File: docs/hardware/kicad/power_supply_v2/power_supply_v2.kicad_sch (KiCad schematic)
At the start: 99 parts, among them J1 Barrel_Jack, J2 LOAD 3V3, J3 LOAD 5V, J4 LOAD Vvar, Q1 MMBT3904LT1G, Q2 AO3401A, SW2 Rotary_Encoder_3_Pin, U1 TPS54302, U14 SHT31-DIS, U15 SHT31-DIS, U2 MCP1700T-3302E/TT, U3 MCP1700T-3302E/TT, U4 TPS54302, U5 MCP1700T-5002E/TT, U6 TPS54302, U7 TPS54302, U8 TPS22917DBV, U9 TPS22917DBV

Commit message: updated schematic for LC filters and added voltage injection to other bucks
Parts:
- removed C11, C18, C9: 1μF, symbol Library:C_Small
- removed D2: B340A-13-F, digikey-footprints:DO-214AC, symbol Library:B340A-13-F
- removed U3: MCP1700T-3302E/TT, digikey-footprints:SOT-23-3, symbol Library:MCP1700T-3302E_TT
- added C10, C19, C32, C33: 10μF, symbol Library:C_Small
- added L2, L4, L7: 1μH, symbol Library:L_Iron
- added R4: 62kR, symbol Library:R_Small_US
- added R9: 82kR, symbol Library:R_Small_US
- R3: value 19kR2 -> 22kR1
- R8: renamed from R7; value 12kR1 -> 13kR3
- renumbered C12 to C11, C13 to C12, C14 to C13, C15 to C14, C16 to C15, C17 to C16, C19 to C17, C20 to C18, C21 to C20, C22 to C21, C23 to C22, C24 to C23, C25 to C24, C26 to C25, C27 to C26, C28 to C27, C29 to C28, C30 to C29, C31 to C30, C32 to C31, C33 to C34, C34 to C35, C35 to C36, C36 to C37, C37 to C38, C38 to C39, C39 to C40, C40 to C41, C41 to C42, C10 to C9, L2 to L3, L3 to L5, L4 to L6, R8 to R10, R9 to R11, R10 to R12, R11 to R13, R12 to R14, R13 to R15, R14 to R16, R15 to R17, R16 to R18, R17 to R19, R18 to R20, R19 to R21, R20 to R22, R21 to R23, R22 to R24, R23 to R25, R24 to R26, R25 to R27, R4 to R5, R5 to R6, R6 to R7
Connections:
- net +3V3B: now also C10.1, L2.2
- net +3V7: now also L2.1
- net +5V5: now also L4.1
- net +5VA: now also C18.1, U5.2 (OUT)
- net +5VB: now also C19.1, L4.2; no longer C18.1, U5.2 (OUT)
- net +V_{VAR}: now also L7.1; no longer Q2.2 (S), R25.2
- net BUCK_12V_EN: now also R11.1; no longer R11.2
- net GNDREF: now also C10.2, C19.2, C32.2, C33.2
- net Microcontroller/BUCK_VVAR_EN_PC5: now also R15.1; no longer R15.2
- net at C7.2, R2.2, R3.1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: now also R4.1
- net at C16.2, R7.2, R8.1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: now also R9.1
- net at U7.5 (EN): now also R15.2; no longer R15.1
- net at U6.5 (EN): now also R11.2; no longer R11.1
- new net: C32.1, C33.1, L7.2, Q2.2 (S), R25.2
- new net DAC_3V7_PA6: R4.2
- new net DAC_5V5_PA5: R9.2
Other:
- sheet Microcontroller ports: added DAC_3V7_PA6, DAC_5V5_PA5; removed none
- note added: "TODO: rework power rails to rely on filtering via inductor and capacitor"
- note removed: "V_{f(MAX)}=0V5"
- moved on the sheet: C17, C18, C8, C9, DS3, DS4, R10, R14, R18, R5, U14, U15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

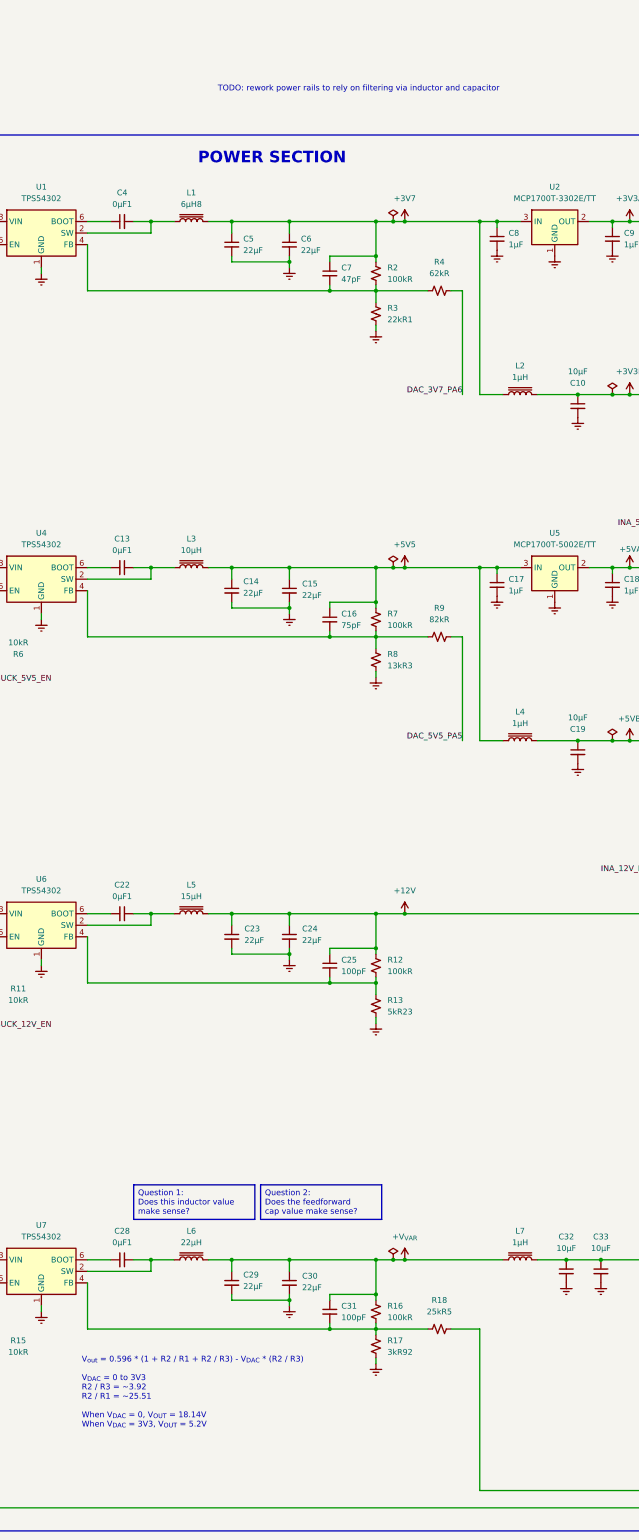
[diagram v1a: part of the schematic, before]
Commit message: rework buck resistor divider values + add fb injection to 3V3 and 5V rail bucks
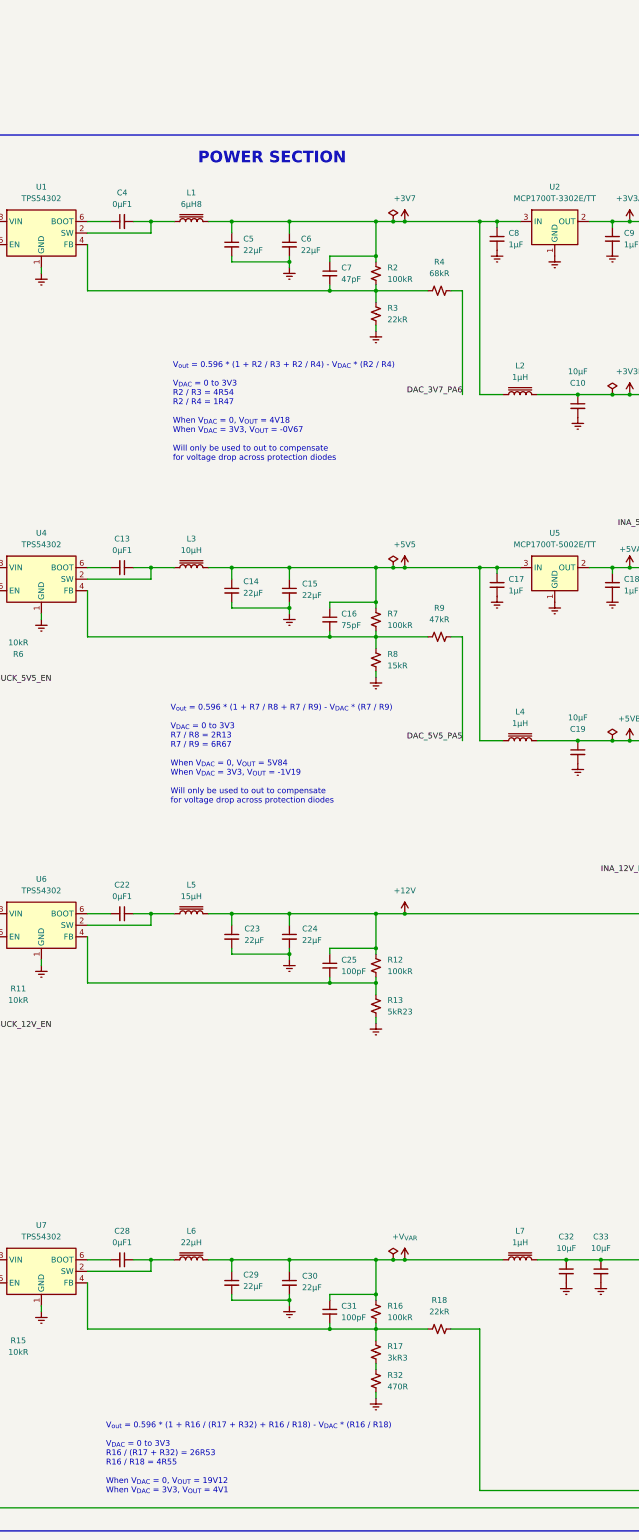
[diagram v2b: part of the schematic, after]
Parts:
- added R32: 470R, symbol Library:R_Small_US
- R17: value 3kR92 -> 3kR3
- R18: value 25kR5 -> 22kR
- R3: value 22kR1 -> 22kR
- R4: value 62kR -> 68kR
- R8: value 13kR3 -> 15kR
- R9: value 82kR -> 47kR
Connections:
- net GNDREF: now also R32.2; no longer R17.2
- new net: R17.2, R32.1
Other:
- note added: "V_{out} = 0.596 * (1 + R16 / (R17 + R32) + R16 / R18) - V_{DAC} * (R16 / R18) V_{DAC} = 0 to 3V3 R16 / (R17 + R32) = 26R53 R16 / R18 = 4R55 When V_{DAC} = 0, V_{OUT} = 19V12 When V_{DAC} = 3V3, V_{OUT} = 4V1"
- note added: "V_{out} = 0.596 * (1 + R2 / R3 + R2 / R4) - V_{DAC} * (R2 / R4) V_{DAC} = 0 to 3V3 R2 / R3 = 4R54 R2 / R4 = 1R47 When V_{DAC} = 0, V_{OUT} = 4V18 When V_{DAC} = 3V3, V_{OUT} = -0V67 Will only be used to out to compensate for voltage drop across protection diodes"
- note added: "V_{out} = 0.596 * (1 + R7 / R8 + R7 / R9) - V_{DAC} * (R7 / R9) V_{DAC} = 0 to 3V3 R7 / R8 = 2R13 R7 / R9 = 6R67 When V_{DAC} = 0, V_{OUT} = 5V84 When V_{DAC} = 3V3, V_{OUT} = -1V19 Will only be used to out to compensate for voltage drop across protection diodes"
- note removed: "TODO: rework power rails to rely on filtering via inductor and capacitor"
- note removed: "V_{out} = 0.596 * (1 + R2 / R1 + R2 / R3) - V_{DAC} * (R2 / R3) V_{DAC} = 0 to 3V3 R2 / R3 = ~3.92 R2 / R1 = ~25.51 When V_{DAC} = 0, V_{OUT} = 18.14V When V_{DAC} = 3V3, V_{OUT} = 5.2V"
- moved on the sheet: R17
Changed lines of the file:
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@@
 	(title_block
 		(title "Digital Variable DC Bench Power Supply")
-		(date "2026-04-27")
-		(rev "1")
+		(date "2026-04-30")
+		(rev "A2")
 	)
 	(rectangle
@@
 		)
 	)
-	(text "V_{out} = 0.596 * (1 + R2 / R1 + R2 / R3) - V_{DAC} * (R2 / R3)\n\nV_{DAC} = 0 to 3V3\nR2 / R3 = ~3.92\nR2 / R1 = ~25.51\n\nWhen V_{DAC} = 0, V_{OUT} = 18.14V\nWhen V_{DAC} = 3V3, V_{OUT} = 5.2V"
+	(text "V_{out} = 0.596 * (1 + R16 / (R17 + R32) + R16 / R18) - V_{DAC} * (R16 / R18)\n\nV_{DAC} = 0 to 3V3\nR16 / (R17 + R32) = 26R53\nR16 / R18 = 4R55\n\nWhen V_{DAC} = 0, V_{OUT} = 19V12\nWhen V_{DAC} = 3V3, V_{OUT} = 4V1"
 		(exclude_from_sim no)
-		(at 124.46 346.71 0)
+		(at 129.794 361.188 0)
 		(effects
 			(font
@@
 		)
 	)
-	(text "TODO: rework power rails to rely on filtering via inductor and capacitor"
-		(exclude_from_sim no)
-		(at 185.42 59.69 0)
-		(effects
-			(font
-				(size 1.27 1.27)
-			)
-		)
-	)
 	(text "V_{f(MAX)}=0V7"
 		(exclude_from_sim no)
@@
 		)
 	)
+	(text "V_{out} = 0.596 * (1 + R2 / R3 + R2 / R4) - V_{DAC} * (R2 / R4)\n\nV_{DAC} = 0 to 3V3\nR2 / R3 = 4R54\nR2 / R4 = 1R47\n\nWhen V_{DAC} = 0, V_{OUT} = 4V18\nWhen V_{DAC} = 3V3, V_{OUT} = -0V67\n\nWill only be used to out to compensate\nfor voltage drop across protection diodes"
+		(exclude_from_sim no)
+		(at 144.526 130.81 0)
+		(effects
+			(font
+				(size 1.27 1.27)
+			)
+			(justify left)
+		)
+	)
 	(text "USER\nINTERFACES"
 		(exclude_from_sim no)
@@
 		)
 	)
+	(text "V_{out} = 0.596 * (1 + R7 / R8 + R7 / R9) - V_{DAC} * (R7 / R9)\n\nV_{DAC} = 0 to 3V3\nR7 / R8 = 2R13\nR7 / R9 = 6R67\n\nWhen V_{DAC} = 0, V_{OUT} = 5V84\nWhen V_{DAC} = 3V3, V_{OUT} = -1V19\n\nWill only be used to out to compensate\nfor voltage drop across protection diodes"
+		(exclude_from_sim no)
+		(at 144.018 206.248 0)
+		(effects
+			(font
+				(size 1.27 1.27)
+			)
+			(justify left)
+		)
+	)
 	(text "No pull-up resistors included for I2C\nbecause the OLED and SHT31s are modules\nwith built-in resistors. May need to\nalter modules or remove the resistors."
 		(exclude_from_sim no)
@@
 		)
 	)
-	(text_box "Question 2:\nDoes the feedforward cap value make sense?"
-		(exclude_from_sim no)
-		(at 163.83 300.99 0)
-		(size 26.67 7.62)
-		(margins 0.9525 0.9525 0.9525 0.9525)
-		(stroke
-			(width 0)
-			(type solid)
-		)
-		(fill
-			(type none)
-		)
-		(effects
-			(font
-				(size 1.27 1.27)
-			)
-			(justify left top)
-		)
-	)
-	(text_box "Question 1:\nDoes this inductor value make sense?"
-		(exclude_from_sim no)
-		(at 135.89 300.99 0)
-		(size 26.67 7.62)
-		(margins 0.9525 0.9525 0.9525 0.9525)
-		(stroke
-			(width 0)
-			(type solid)
-		)
-		(fill
-			(type none)
-		)
-		(effects
-			(font
-				(size 1.27 1.27)
-			)
-			(justify left top)
-		)
-	)
 	(junction
 		(at 539.75 24.13)
@@
 	(wire
 		(pts
+			(xy 189.23 340.36) (xy 189.23 341.63)
+		)
+		(stroke
+			(width 0)
+			(type default)
+		)
+	)
+	(wire
+		(pts
 			(xy 408.94 48.26) (xy 414.02 48.26)
 		)
@@
 	(wire
 		(pts
-			(xy 189.23 332.74) (xy 189.23 334.01)
+			(xy 189.23 332.74) (xy 189.23 335.28)
 		)
 		(stroke
@@
 	(wire
 		(pts
-			(xy 189.23 339.09) (xy 189.23 340.36)
-		)
-		(stroke
-			(width 0)
-			(type default)
-		)
-	)
-	(wire
-		(pts
 			(xy 260.35 165.1) (xy 261.62 165.1)
 		)
@@
 	(wire
 		(pts
+			(xy 189.23 346.71) (xy 189.23 347.98)
+		)
+		(stroke
+			(width 0)
+			(type default)
+		)
+	)
+	(wire
+		(pts
 			(xy 193.04 165.1) (xy 195.58 165.1)
 		)
@@
 	)
 	(symbol
+		(lib_id "Library:R_Small_US")
+		(at 189.23 344.17 0)
+		(unit 1)
+		(exclude_from_sim no)
+		(in_bom yes)
+		(on_board yes)
+		(dnp no)
+		(fields_autoplaced yes)
+		(property "Reference" "R32"
+			(at 191.77 342.8999 0)
+			(effects
+				(font
+					(size 1.27 1.27)
+				)
+				(justify left)
+			)
+		)
+		(property "Value" "470R"
+			(at 191.77 345.4399 0)
+			(effects
+				(font
+					(size 1.27 1.27)
+				)
+				(justify left)
+			)
+		)
+		(property "Footprint" ""
+			(at 189.23 344.17 0)
+			(effects
+				(font
+					(size 1.27 1.27)
+				)
+				(hide yes)
+			)
+		)
+		(property "Datasheet" "~"
+			(at 189.23 344.17 0)
+			(effects
+				(font
+					(size 1.27 1.27)
+				)
+				(hide yes)
+			)
+		)
+		(property "Description" "Resistor, small US symbol"
+			(at 189.23 344.17 0)
+			(effects
+				(font
+					(size 1.27 1.27)
+				)
+				(hide yes)
+			)
+		)
+		(pin "1"
+		)
+		(pin "2"
+		)
+		(instances
+			(project "power_supply_v2"
+				(path "/cac0009d-9d0b-438f-a386-67368a9db47f"
+					(reference "R32")
+					(unit 1)
+				)
+			)
+		)
+	)
+	(symbol
 		(lib_id "power:PWR_FLAG")
 		(at 40.64 43.18 0)
@@
 			)
 		)
-		(property "Value" "22kR1"
+		(property "Value" "22kR"
 			(at 191.77 110.4899 0)
 			(effects
@@
 	(symbol
 		(lib_id "power:GNDREF")
-		(at 189.23 340.36 0)
+		(at 189.23 347.98 0)
 		(unit 1)
 		(exclude_from_sim no)
@@
 		(fields_autoplaced yes)
 		(property "Reference" "#PWR011"
-			(at 189.23 346.71 0)
+			(at 189.23 354.33 0)
 			(effects
 				(font
@@
 		)
 		(property "Value" "GNDREF"
-			(at 189.23 345.44 0)
+			(at 189.23 353.06 0)
 			(effects
 				(font
@@
 		)
 		(property "Footprint" ""
-			(at 189.23 340.36 0)
+			(at 189.23 347.98 0)
 			(effects
 				(font
@@
 		)
 		(property "Datasheet" ""
-			(at 189.23 340.36 0)
+			(at 189.23 347.98 0)
 			(effects
 				(font
@@
 		)
 		(property "Description" "Power symbol creates a global label with name \"GNDREF\" , reference supply ground"
-			(at 189.23 340.36 0)
+			(at 189.23 347.98 0)
 			(effects
 				(font
@@
 			)
 		)
-		(property "Value" "82kR"
+		(property "Value" "47kR"
 			(at 203.2 176.53 90)
 			(effects
@@
 			)
 		)
-		(property "Value" "62kR"
+		(property "Value" "68kR"
 			(at 203.2 100.33 90)
 			(effects
@@
 			)
 		)
-		(property "Value" "13kR3"
+		(property "Value" "15kR"
 			(at 191.77 186.69 0)
 			(effects
@@
 	(symbol
 		(lib_id "Library:R_Small_US")
-		(at 189.23 336.55 0)
+		(at 189.23 337.82 0)
 		(unit 1)
 		(exclude_from_sim no)
@@
 		(fields_autoplaced yes)
 		(property "Reference" "R17"
-			(at 191.77 335.2799 0)
+			(at 191.77 336.5499 0)
 			(effects
 				(font
@@
 			)
 		)
-		(property "Value" "3kR92"
-			(at 191.77 337.8199 0)
+		(property "Value" "3kR3"
+			(at 191.77 339.0899 0)
 			(effects
 				(font
@@
 		)
 		(property "Footprint" ""
-			(at 189.23 336.55 0)
+			(at 189.23 337.82 0)
 			(effects
 				(font
@@
 		)
 		(property "Datasheet" "~"
-			(at 189.23 336.55 0)
+			(at 189.23 337.82 0)
 			(effects
 				(font
@@
 		)
 		(property "Description" "Resistor, small US symbol"
-			(at 189.23 336.55 0)
+			(at 189.23 337.82 0)
 			(effects
 				(font
@@
 			)
 		)
-		(property "Value" "25kR5"
+		(property "Value" "22kR"
 			(at 203.2 328.93 90)
 			(effects

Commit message: remove redundant switches for variable rail
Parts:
- removed Q1: MMBT3904LT1G, digikey-footprints:SOT-23-3, symbol Library:MMBT3904LT1G
- removed Q2: AO3401A, digikey-footprints:SOT-23-3, symbol Library:AO3401A
- removed R14: 10mR, symbol Library:R_Small_US
- removed R23, R25: 1kR, symbol Library:R_Small_US
- removed R24, R26: 10kR, symbol Library:R_Small_US
- removed S1: ~, symbol Library:Button_Array_4
- added S2: SW_Button_4, symbol Library:Button_Array_4
- S1: renamed from SW2; value Rotary_Encoder_3_Pin -> Rotary_Encoder_3
- U2: value MCP1700T-3302E/TT -> MCP1700T
- U5: value MCP1700T-5002E/TT -> MCP1700T
- renumbered R15 to R14, R16 to R15, R17 to R16, R32 to R17, U14 to U16, U15 to U17
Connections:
- net GNDREF: now also S2.5 (GND)
- net INA_V_{VAR}_IN+: now also C32.1, C33.1, L7.2
- net Microcontroller/BTN_3V3B_PB7: now also S2.1 (B1)
- net Microcontroller/BTN_5VB_PC13: now also S2.2 (B2)
- net Microcontroller/BTN_DSP_PC15: now also S2.4 (B4)
- net Microcontroller/BTN_VVAR_PC14: now also S2.3 (B3)
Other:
- sheet Current_Sensors ports: added none; removed INA_12V_IN+, INA_12V_IN-, INA_12V_OUT_PB13
- sheet Microcontroller ports: added none; removed INA_12V_OUT_PB13, NPN_V_{VAR}_PA0
- note added: "MCU & peripherals power"
- note added: "V_{out} = 0.596 * (1 + R15 / (R16 + R17) + R15 / R18) - V_{DAC} * (R15 / R18) V_{DAC} = 0 to 3V3 R15 / (R16 + R17) = 26R53 R15 / R18 = 4R55 When V_{DAC} = 0, V_{OUT} = 19V12 When V_{DAC} = 3V3, V_{OUT} = 4V1"
- note added: "fan power"
- note added: "voltage buffer for fan PWM and LED data"
- note removed: "V_{out} = 0.596 * (1 + R16 / (R17 + R32) + R16 / R18) - V_{DAC} * (R16 / R18) V_{DAC} = 0 to 3V3 R16 / (R17 + R32) = 26R53 R16 / R18 = 4R55 When V_{DAC} = 0, V_{OUT} = 19V12 When V_{DAC} = 3V3, V_{OUT} = 4V1"
- moved on the sheet: C1, C42, D1, D7, D8, J1, J4, R1, R27, S1, U16, U17

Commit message: Rev a4 (#8)
* update schematic to fix power rail node and update resistors to reflect series to reach target dividers

* rev 4A for schematic to reflect changes from assembling

* update schematic and README

---------

Co-authored-by: chris <chris@laptop.malecki.com>
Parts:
- removed R10: 25mR, symbol Library:R_Small_US
- removed R19: 10R, symbol Library:R_Small_US
- added C24: 0μF1, symbol Library:C_Small
- added D4: WS2812, LED_SMD:LED_WS2812B-2020_PLCC4_2.0x2.0mm, symbol Library:WS2812B-2020
- added M1: Fan_4pin, symbol Library:Fan_4pin
- added R12, R13, R15, R16, R6: 10kR, symbol Library:R_Small_US
- added R14: 470R, symbol Library:R_Small_US
- added U10: NUCLEO-G474RE, NUCLEO-G474RE:MODULE_NUCLEO-G474RE, symbol Library:NUCLEO-G474RE
- added U11, U12: INA180A3, Package_TO_SOT_SMD:SOT-23-5, symbol Library:INA180A3
- added U13: INA180A1, Package_TO_SOT_SMD:SOT-23-5, symbol Library:INA180A3
- added U6: SN74AHCT125N, digikey-footprints:DIP-14_W3mm, symbol Library:SN74AHCT125N
- C43: renamed from C42; value 47μF -> 22μF
- DS1: renamed from DS3; value OLED_96in_64x128_I2C -> OLED_64x128_I2C
- DS2: renamed from DS4; value OLED_96in_64x128_I2C -> OLED_64x128_I2C
- R20: renamed from R13; value 5kR23 -> 4kR7
- R21: value 10R -> 470R
- renumbered C34 to C11, C35 to C12, C36 to C13, C37 to C14, C11 to C15, C12 to C16, C13 to C17, C14 to C18, C15 to C19, C16 to C20, C17 to C21, C18 to C22, C19 to C23, C38 to C25, C39 to C26, C40 to C27, C41 to C28, C20 to C29, C21 to C30, C22 to C31, C23 to C32, C24 to C33, C25 to C34, C26 to C35, C27 to C36, C28 to C37, C29 to C38, C30 to C39, C31 to C40, C32 to C41, C33 to C42, D4 to D2, D6 to D5, D5 to D6, D8 to D7, D7 to D8, R8 to R10, R9 to R11, R22 to R17, R11 to R18, R12 to R19, R14 to R22, R15 to R23, R16 to R24, R17 to R25, R18 to R26, R20 to R7, R6 to R8, R7 to R9, U16 to U14, U17 to U15, U8 to U3, U9 to U7, U6 to U8, U7 to U9
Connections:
- net +12V: now also M1.2 (+)
- net +20V: now also U11.4 (-)
- net +3.3VA: now also R15.1
- net +3V3A: now also U10.CN7_16 (+3V3), U11.5 (V+), U12.5 (V+), U13.5 (V+)
- net +5VA: now also C24.1, D4.4 (VDD), U6.14 (VCC)
- net DAC_3V7_PA6: now also U10.CN10_13 (PA6)
- net DAC_5V5_PA5: now also U10.CN10_11 (PA5)
- net GNDREF: now also C24.2, D4.2 (VSS), M1.1 (-), R12.2, R13.2, R16.2, R6.2, U10.CN7_8 (GND_CN7_8), U11.2 (GND), U12.2 (GND), U13.2 (GND), U6.10 (3~{OE}), U6.12 (4A), U6.13 (4~{OE}), U6.7 (GND), U6.9 (3A); no longer D3.K, D6.K, D8.K, R20.2
- net INA_5VB_IN+: now also D6.K, U13.3 (+); no longer C27.1, C28.1, D5.2 (A2), D6.A, R21.1, U7.5 (QOD), U7.6 (VOUT)
- net INA_5VB_IN-: now also U13.4 (-)
- net INA_V_{VAR}_IN+: now also D8.K, U12.3 (+); no longer C41.1, C42.1, C43.1, D7.2 (A2), D8.A, L7.2
- net INA_V_{VAR}_IN-: now also U12.4 (-)
- net at C13.1, C14.1, D2.2 (A2)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: no longer R7.1
- net BUCK_12V_EN renamed BUCK_12V_EN_PC6
- net BUCK_12V_EN_PC6: now also U10.CN10_4 (PC6)
- net BUCK_5V5_EN renamed BUCK_5V5_EN_PC8
- net BUCK_5V5_EN_PC8: now also U10.CN10_2 (PC8)
- net Current_Sensors/INA_20V_IN+ renamed INA_20V_IN+
- net INA_20V_IN+: now also U11.3 (+)
- net HS_SW_3V3B_ON renamed HS_SW_3V3B_PC2
- net HS_SW_3V3B_PC2: now also R6.1, U10.CN7_35 (PC2)
- net HS_SW_5VB_ON renamed HS_SW_5VB_PC3
- net HS_SW_5VB_PC3: now also R16.1, U10.CN7_37 (PC3)
- net Microcontroller/BTN_3V3B_PB7 renamed BTN_3V3B_PB7
- net BTN_3V3B_PB7: now also U10.CN7_21 (PB7)
- net Microcontroller/BTN_5VB_PC13 renamed BTN_5VB_PC13
- net BTN_5VB_PC13: now also U10.CN7_23 (PC13)
- net Microcontroller/BTN_DSP_PC15 renamed BTN_DSP_PC15
- net BTN_DSP_PC15: now also U10.CN7_27 (PC15)
- net Microcontroller/BTN_VVAR_PC14 renamed BTN_V_{VAR}_PC14
- net BTN_V_{VAR}_PC14: now also U10.CN7_25 (PC14)
- net Microcontroller/BUCK_VVAR_EN_PC5 renamed BUCK_V_{VAR}_EN_PC5
- net BUCK_V_{VAR}_EN_PC5: now also U10.CN10_6 (PC5)
- net Microcontroller/DAC_V_{VAR}_PA4 renamed DAC_V_{VAR}_PA4
- net DAC_V_{VAR}_PA4: now also U10.CN7_32 (PA4)
- net Microcontroller/I2C1_SCL_PB8 renamed I2C1_SCL_PB8
- net I2C1_SCL_PB8: now also U14.4 (SCL), U10.CN10_3 (PB8); no longer DS2.4 (SCL)
- net Microcontroller/I2C1_SDA_PB9 renamed I2C1_SDA_PB9
- net I2C1_SDA_PB9: now also U14.1 (SDA), U10.CN10_5 (PB9); no longer DS2.3 (SDA)
- net Microcontroller/I2C2_SCL_PA9 renamed I2C2_SCL_PA9
- net I2C2_SCL_PA9: now also DS2.4 (SCL), U10.CN10_21 (PA9); no longer U14.4 (SCL)
- net Microcontroller/I2C2_SDA_PA8 renamed I2C2_SDA_PA8
- net I2C2_SDA_PA8: now also DS2.3 (SDA), U10.CN10_23 (PA8); no longer U14.1 (SDA)
- net Microcontroller/OPAMP_3V3A_PA1 renamed OPAMP_3V3A_PA1
- net OPAMP_3V3A_PA1: now also U10.CN7_30 (PA1)
- net Microcontroller/OPAMP_3V3B_PA7 renamed OPAMP_3V3B_PA7
- net OPAMP_3V3B_PA7: now also U10.CN10_15 (PA7)
- net Microcontroller/RTRY_CLK_PB5 renamed RTRY_CLK_PB5
- net RTRY_CLK_PB5: now also U10.CN10_29 (PB5)
- net Microcontroller/RTRY_DT_PB4 renamed RTRY_DT_PB4
- net RTRY_DT_PB4: now also U10.CN10_27 (PB4)
- net Microcontroller/RTRY_SW_PB10 renamed RTRY_SW_PB10
- net RTRY_SW_PB10: now also U10.CN10_25 (PB10)
- new net: D3.K, R7.1
- new net: C41.1, C42.1, C43.1, D7.2 (A2), D8.A, L7.2
- new net: D4.3 (DIN), R14.1
- new net: R14.2, U6.3 (1Y)
- new net: C27.1, C28.1, D5.2 (A2), D6.A, U7.5 (QOD), U7.6 (VOUT)
- new net: M1.4 (PWM), U6.6 (2Y)
- new net: R20.2, R21.1
- new net: R13.1, U6.1 (1~{OE})
- new net: R12.1, U6.4 (2~{OE})
- new net FAN_PWM_PA12: U10.CN10_12 (PA12), U6.5 (2A)
- new net FAN_TACH_PA11: M1.3 (Tacho), R15.2, U10.CN10_14 (PA11)
- new net INA_20V_OUT_PB0: U10.CN7_34 (PB0), U11.1
- new net INA_5VB_OUT_PB12: U10.CN10_16 (PB12), U13.1
- new net INA_V_{VAR}_OUT_PB14: U10.CN10_28 (PB14), U12.1
- new net LED_DATA_PC9: U10.CN10_1 (PC9), U6.2 (1A)
- no-connect marks 5 -> 48
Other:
- removed sheet Buffer_Fan_LEDs
- removed sheet Current_Sensors
- removed sheet Microcontroller
- note added: "4x LED series"
- note added: "GND"
- note added: "IN+"
- note added: "IN-"
- note added: "LOADS"
- note added: "MCU"
- note added: "OUT"
- note added: "POWER/BUCKS"
- note added: "Pin assignment is not optimized or based on any physical layout currently."
- note added: "REGULATION"
- note added: "SWITCHES"
- note added: "VS"
- note added: "V_{out} = 0.596 * (1 + R2 / R3 + R2 / R4) - V_{DAC} * (R2 / R4) V_{DAC} = 0 to 3V3 R2 / R3 = 4R54 R2 / R4 = 1R47 When V_{DAC} = 0, V_{OUT} = 4V18 When V_{DAC} = 3V3, V_{OUT} = -0V67"
- note added: "V_{out} = 0.596 * (1 + R7 / R8 + R7 / R9) - V_{DAC} * (R7 / R9) V_{DAC} = 0 to 3V3 R7 / R8 = 2R13 R7 / R9 = 6R67 When V_{DAC} = 0, V_{OUT} = 5V84 When V_{DAC} = 3V3, V_{OUT} = -1V19"
- note removed: "MCU & peripherals power"
- note removed: "POWER SECTION"
- note removed: "SWITCHES & LOADS"
- note removed: "V_{f(MAX)}=0V7"
- note removed: "V_{out} = 0.596 * (1 + R2 / R3 + R2 / R4) - V_{DAC} * (R2 / R4) V_{DAC} = 0 to 3V3 R2 / R3 = 4R54 R2 / R4 = 1R47 When V_{DAC} = 0, V_{OUT} = 4V18 When V_{DAC} = 3V3, V_{OUT} = -0V67 Will only be used to out to compensate for voltage drop across protection diodes"
- note removed: "V_{out} = 0.596 * (1 + R7 / R8 + R7 / R9) - V_{DAC} * (R7 / R9) V_{DAC} = 0 to 3V3 R7 / R8 = 2R13 R7 / R9 = 6R67 When V_{DAC} = 0, V_{OUT} = 5V84 When V_{DAC} = 3V3, V_{OUT} = -1V19 Will only be used to out to compensate for voltage drop across protection diodes"
- note removed: "voltage buffer for fan PWM and LED data"
- moved on the sheet: C1, C10, C11, C12, C13, C14, C15, C16, C17, C18, C19, C2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

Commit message: C malecki #9 (#10)
* move pins around for better proximity to connection in layout

* initial pinout based on board layout

* copy over some code from v1

* move opamp pins
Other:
- note added: "CURRENT SENSORS"
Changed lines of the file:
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@@
 		)
 	)
-	(text "TEMPERATURE SENSORS"
+	(text "CURRENT SENSORS"
 		(exclude_from_sim no)
-		(at 105.41 367.03 0)
+		(at 102.616 367.03 0)
 		(effects
 			(font
